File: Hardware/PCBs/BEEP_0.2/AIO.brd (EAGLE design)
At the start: 106 x 69.1 mm, 91 parts, among them IC1 74HC238SSOP, IC2 74HC238SSOP, IC3 ULN2803ASOP18, IC4 ULN2803ASOP18, IC5 ATXMEGA64D3-AU, IC6 GY-81, IC7 TB6612FNG, IC8 TS34119SMD, IC9 RASPBERRY-PI, Q1 DMN2075U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

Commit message: change most 0603 components to 0805 change smd Typ D Footprint to THT Footprint
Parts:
- C12, C17: device rcl:C0603 -> resistor:M0805
- C13, C14: value 10uF -> (none); device rcl:SMC_D -> rcl:E2-5
- Q4: device crystal:HC49/S -> crystal:HC18U-V
- R10, R12, R13, R14, R18, R19, R20, R23, R24, R27, R30, R7: device rcl:R0603 -> resistor:M0805
- moved C13 14.4 mm to (26.1, 29.4), turned to 180 degrees
- moved C14 13.7 mm to (39.7, 39.4), turned to 180 degrees
- moved R30 4.78 mm to (43.0, 22.0)
- moved Q7 4.73 mm to (41.5, 30.1)
- moved R23 4.72 mm to (43.1, 24.1)
- moved R24 3.71 mm to (46.2, 19.8), turned to 270 degrees
- moved R12 2.67 mm to (25.0, 46.4)
- moved R27 1.92 mm to (37.0, 30.5)
- moved C17 1.82 mm to (46.2, 15.8), turned to 270 degrees
- moved C16 1.75 mm to (26.2, 25.4)
- moved R19 1.10 mm to (68.6, 18.8)
- moved R10 0.94 mm to (22.6, 46.4)
- moved R8 0.60 mm to (64.1, 61.3)
- moved C11 0.41 mm to (75.5, 30.4)
- moved R18 0.40 mm to (75.4, 28.3)
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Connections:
- net +3V3: now also C14.+; no longer C13.-
- net +7V: now also C13.+; no longer C14.-
- net GND: now also C13.-, C14.-; no longer C13.+, C14.+
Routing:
- net POWER_OFF: track 85.7 -> 93.2 mm
- net MOTOR_B_IN1: track 34.1 -> 26.7 mm
- net MOTOR_B_IN2: track 35.0 -> 27.9 mm
- net +7V: track 217.3 -> 211.6 mm
- net BATT_U: track 48.0 -> 43.7 mm
- net GND: track 684.6 -> 688.1 mm
- net N$16: track 13.2 -> 16.7 mm
- net +3V3: track 408.7 -> 411.3 mm
- net N$22: track 27.2 -> 29.0 mm
- net SDA: track 86.0 -> 84.4 mm
- net SPEAKER_O1: track 93.7 -> 95.1 mm
- net IR_LED_K7_OUT: track 83.6 -> 82.4 mm
- net COLOR_DIODE_2: track 27.9 -> 28.9 mm
- net IR_LED_K2_OUT: track 61.3 -> 60.2 mm
- net IR_LED_K3_OUT: track 39.9 -> 38.9 mm
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
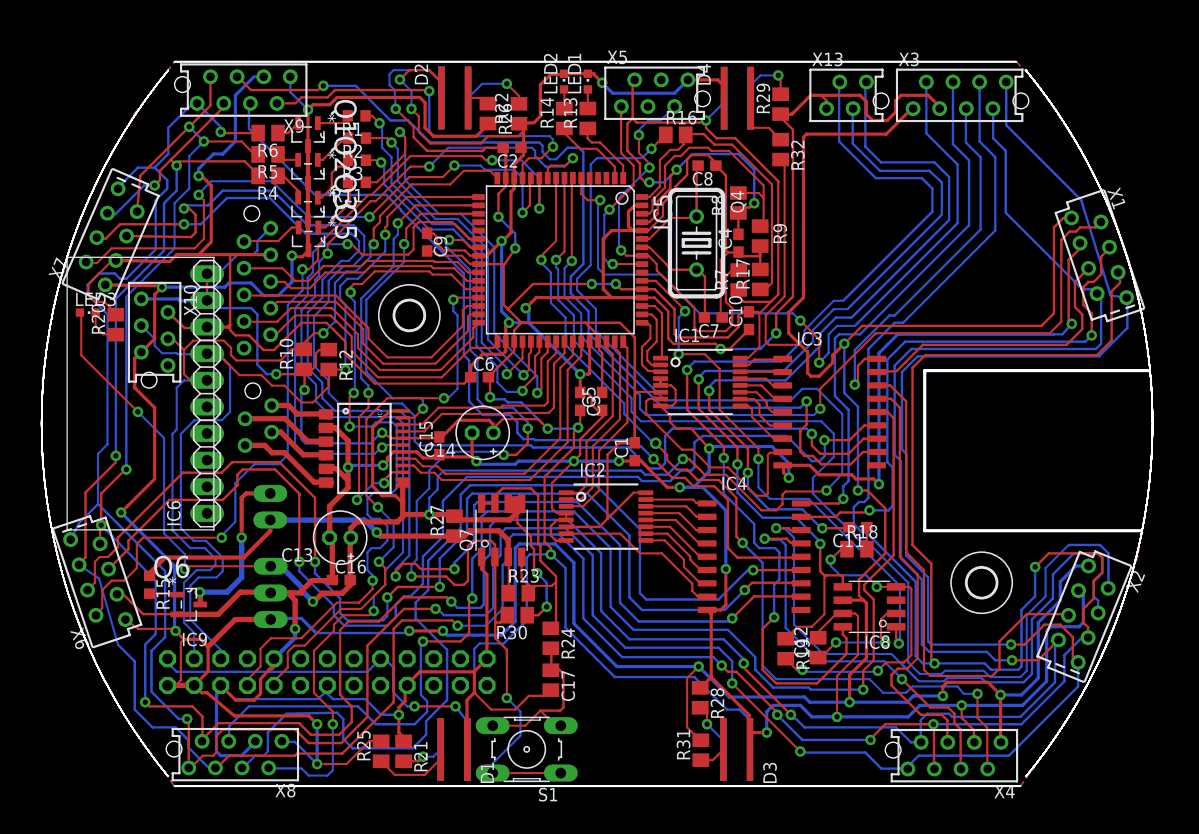
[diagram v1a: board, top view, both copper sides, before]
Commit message: add connections from xmega to encoders enhance Borders
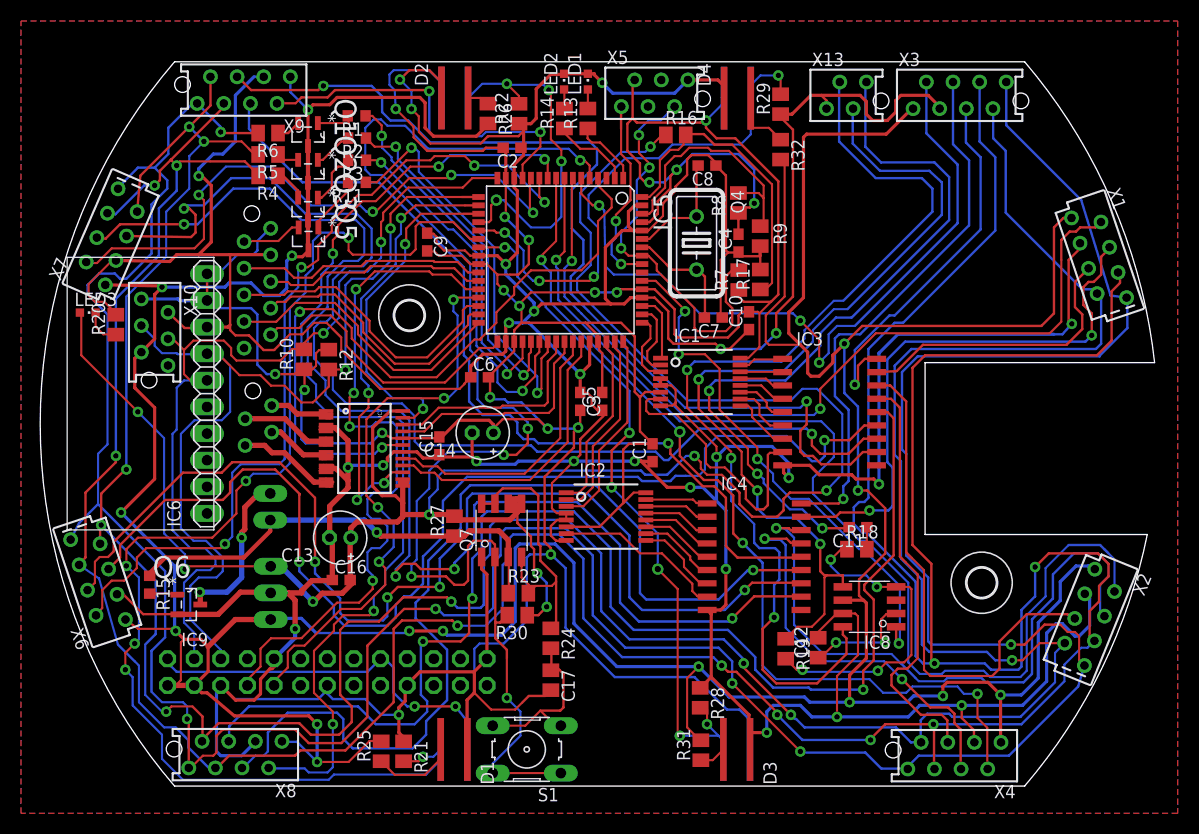
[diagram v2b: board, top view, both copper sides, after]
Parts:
- moved C1 1.70 mm to (55.9, 37.5)
- moved X2 0.67 mm to (97.6, 21.8)
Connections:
- net ENCODER_L1: now also IC5.20
- net ENCODER_L2: now also IC5.21
- net ENCODER_R1: now also IC5.22
- net ENCODER_R2: now also IC5.23
- net MOTOR_STBY: now also IC5.4; no longer IC5.22
- net POWER_OFF: now also IC5.5; no longer IC5.23
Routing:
- net ENCODER_R1: track 4.47 -> 119.5 mm, vias 1 -> 6
- net ENCODER_R2: track 7.13 -> 68.5 mm, vias 1 -> 6
- net ENCODER_L2: track 6.11 -> 50.1 mm, vias 1 -> 4
- net POWER_OFF: track 93.2 -> 129.3 mm
- net ENCODER_L1: track 6.65 -> 34.6 mm, vias 1 -> 4
- net MOTOR_STBY: track 50.4 -> 70.5 mm
- net ADISTANCE_4: track 103.7 -> 97.7 mm
- net +3V3: track 411.3 -> 406.8 mm, vias 18 -> 20
- net COLOR_SENSOR_PWM_LED: track 44.0 -> 39.6 mm
- net N$34: track 22.8 -> 26.0 mm
- net GND: track 688.1 -> 690.4 mm
- net IR_LED_K6_OUT: track 124.7 -> 126.9 mm
- net ADISTANCE_1: track 82.9 -> 80.8 mm
- net ADISTANCE_7: track 36.7 -> 35.0 mm
- net PDI_DATA: track 20.0 -> 18.5 mm
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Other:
- board size 106 x 69.1 mm -> 106.3 x 69.1 mm
